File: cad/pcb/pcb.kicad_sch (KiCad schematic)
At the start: 0 parts

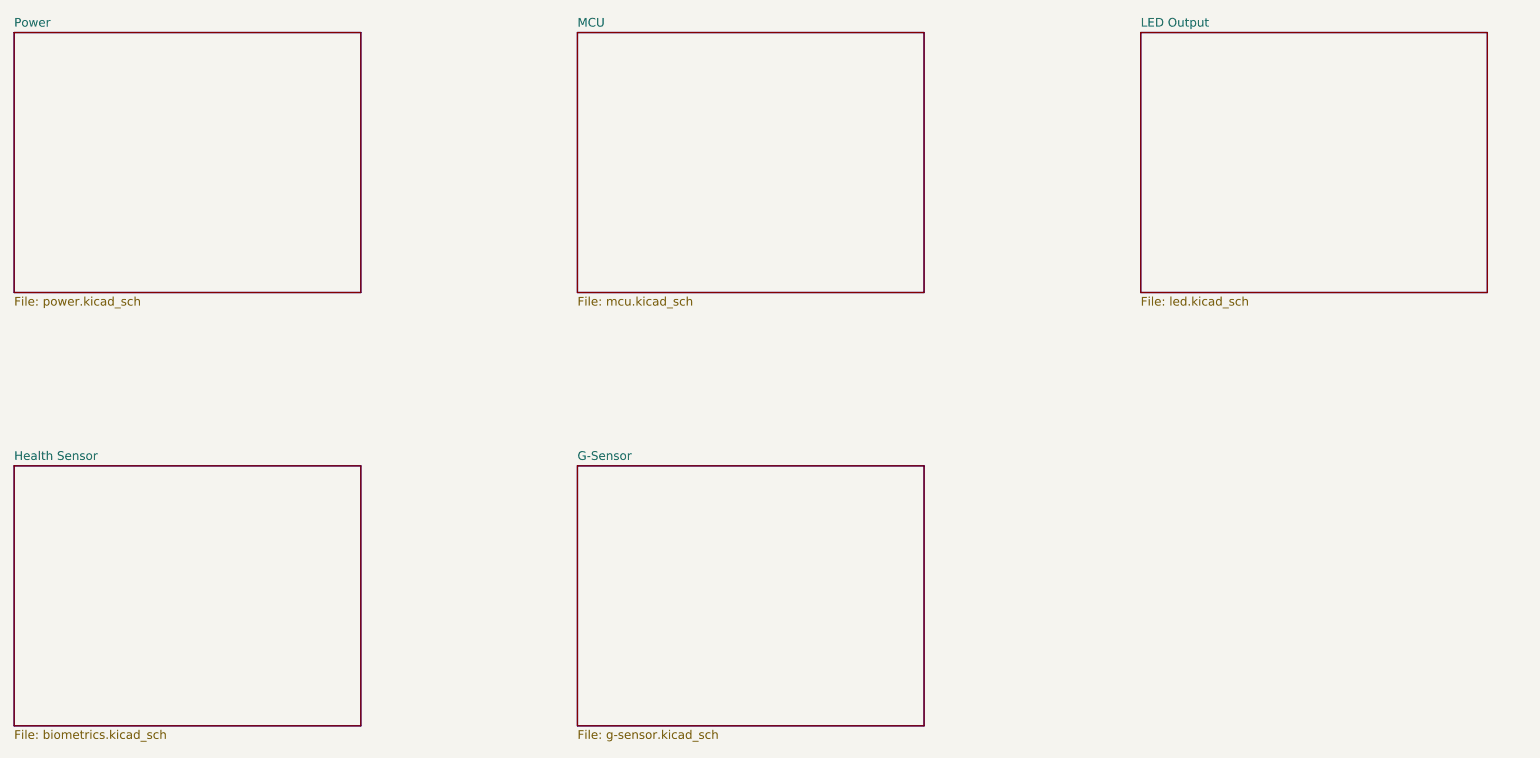
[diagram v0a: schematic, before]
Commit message: finish overview schematic page
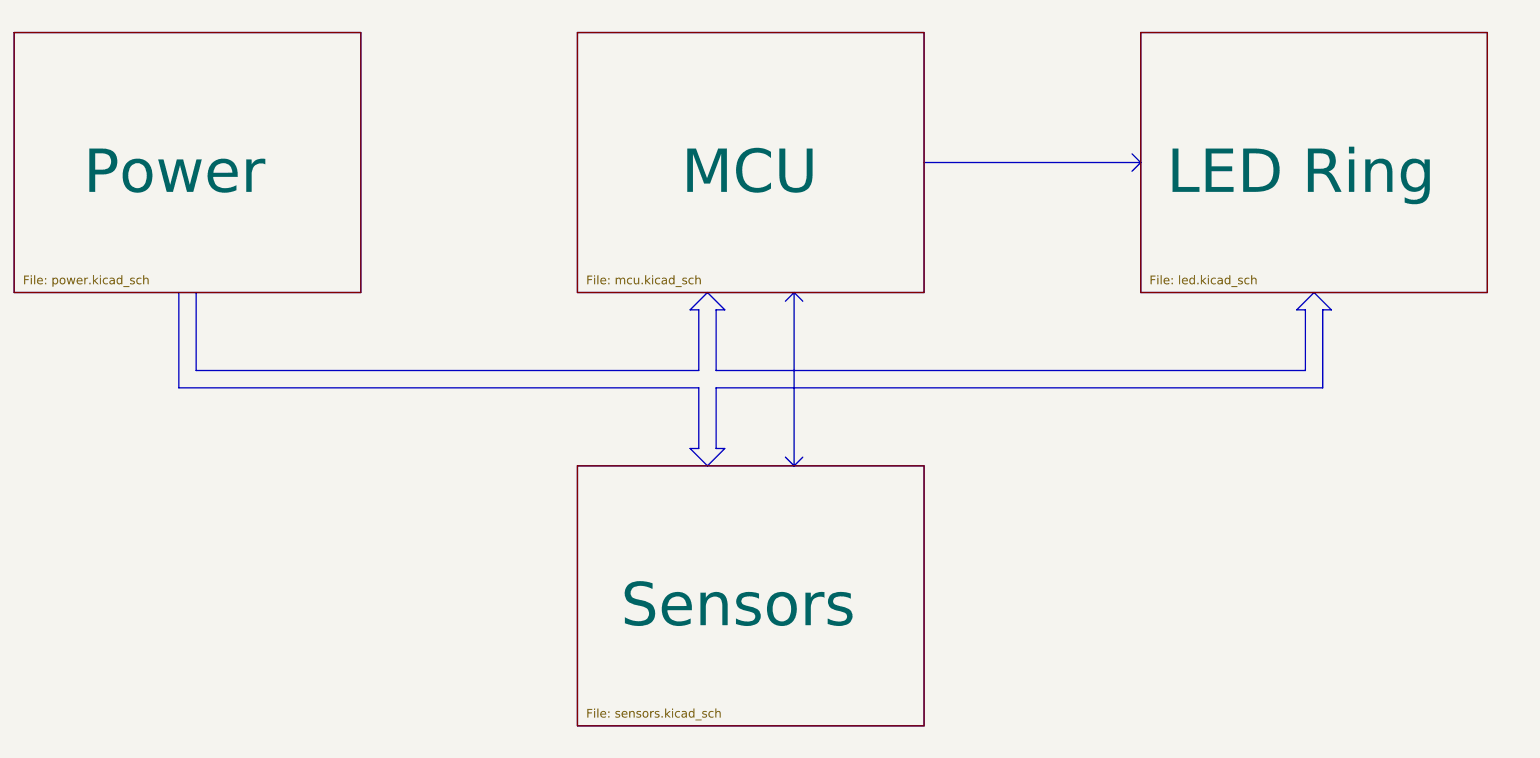
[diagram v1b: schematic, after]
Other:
- sheet G-Sensor renamed Sensors
- sheet LED Output renamed LED Ring
- removed sheet Health Sensor
- sheet Sensors: file g-sensor.kicad_sch -> sensors.kicad_sch
